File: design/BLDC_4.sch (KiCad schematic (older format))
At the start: 29 parts, among them K1 SERVO, P1 HALL, P101 CANBUS, P3 PWR_COMM/USART1/Encoder, P4 IN+, P5 IN-, P6 MOTOR1, P7 MOTOR2, P9 MOTOR3, X1 MINI-USB-SHIELD-32005-201

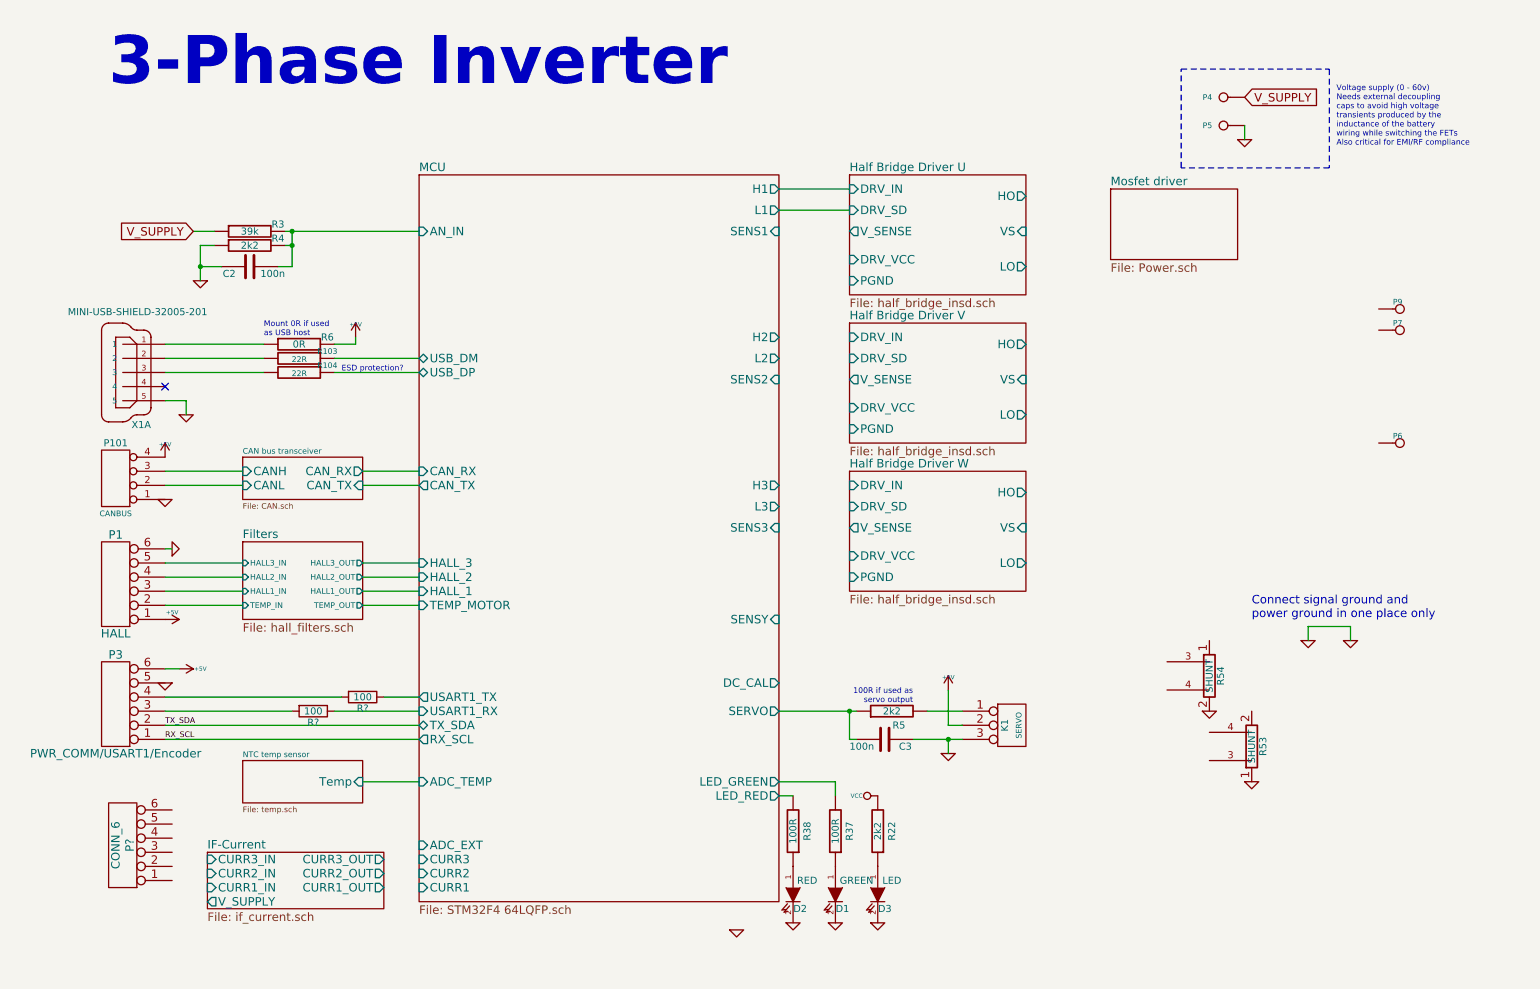
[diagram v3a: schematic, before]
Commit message: Removed 5V power level. Integrated isolated CAN bus driver.
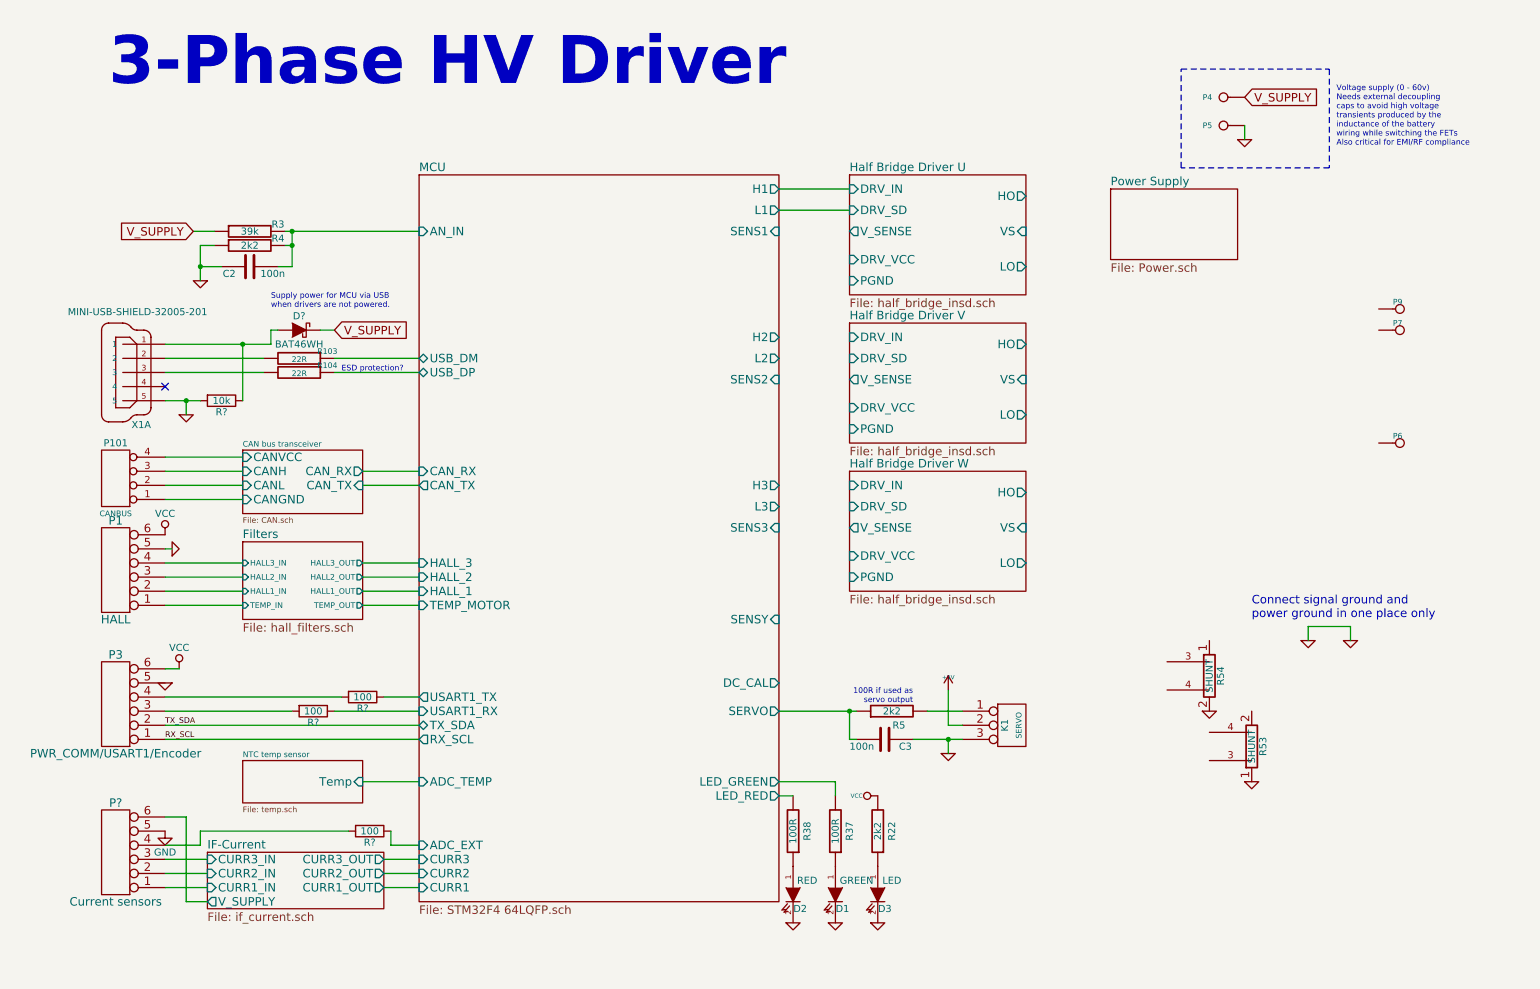
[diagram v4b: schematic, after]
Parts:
- removed R6: 0R, SMD_Packages:SMD-0603_r, symbol R-RESCUE-BLDC_4
- added D?: BAT46WH, symbol BAT46WH
- added R?: 100, symbol R
- added R?: 10k, symbol R
- P?: value CONN_6 -> Current sensors
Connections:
- net +5V: no longer P1.1, P101.4 (P4), P3.6
- net Filters/HALL1_IN: now also P1.2; no longer P1.3
- net Filters/HALL2_IN: now also P1.3; no longer P1.4
- net Filters/HALL3_IN: now also P1.4; no longer P1.5
- net Filters/TEMP_IN: now also P1.1; no longer P1.2
- net GND: now also P1.5, P?.5, R?.2; no longer P1.6, P101.1 (P1)
- net IF-Current/CURR1_IN: now also P?.1
- net IF-Current/CURR2_IN: now also P?.2
- net IF-Current/CURR3_IN: now also P?.3
- net IF-Current/V_SUPPLY: now also P?.6
- net MCU/ADC_EXT: now also R?.1
- net VCC: now also P1.6, P3.6
- net V_SUPPLY: now also D?.1 (K)
- net at X1.1: now also D?.2 (A), R?.1
- net at P?.4: now also R?.2
- new net CAN bus transceiver/CANGND: P101.1 (P1)
- new net CAN bus transceiver/CANVCC: P101.4 (P4)
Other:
- note added: "3-Phase HV Driver"
- note added: "Supply power for MCU via USB\nwhen drivers are not powered."
- note removed: "3-Phase Inverter"
- note removed: "Mount 0R if used\nas USB host"
- moved on the sheet: P1, P?
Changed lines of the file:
@@
 encoding utf-8
 Sheet 1 10
-Title "BLDC Driver 4.6"
-Date "25 Aug 2014"
-Rev "4.6"
-Comp "Benjamin Vedder"
+Title "3-Phase HV Driver"
+Date "2015-08-27"
+Rev "0.1"
+Comp "Jörg Wangemann"
 Comment1 ""
 Comment2 ""
@@
 L CONN_6 P1
 U 1 1 522DA047
-P 1100 4650
-F 0 "P1" H 1100 4300 60  0000 C CNN
-F 1 "HALL" H 1100 5000 60  0000 C CNN
-F 2 "CRF1:MICRO_JST_6" H 1100 4650 60  0001 C CNN
-F 3 "" H 1100 4650 60  0001 C CNN
-	1    1100 4650
+P 1100 4550
+F 0 "P1" H 1100 4200 60  0000 C CNN
+F 1 "HALL" H 1100 4900 60  0000 C CNN
+F 2 "CRF1:MICRO_JST_6" H 1100 4550 60  0001 C CNN
+F 3 "" H 1100 4550 60  0001 C CNN
+	1    1100 4550
 	-1   0    0    1
 $EndComp
 $Comp
-L +5V #PWR01
-U 1 1 522DA04D
-P 1450 4900
-F 0 "#PWR01" H 1450 4990 20  0001 C CNN
-F 1 "+5V" V 1400 4950 30  0000 C CNN
-F 2 "" H 1450 4900 60  0001 C CNN
-F 3 "" H 1450 4900 60  0001 C CNN
-	1    1450 4900
-	0    1    1    0
-$EndComp
-$Comp
 L GND-RESCUE-BLDC_4 #PWR02
 U 1 1 522DA053
@@
 $EndComp
 $Comp
-L +5V #PWR07
-U 1 1 522DA11A
-P 1550 5250
-F 0 "#PWR07" H 1550 5340 20  0001 C CNN
-F 1 "+5V" V 1550 5400 30  0000 C CNN
-F 2 "" H 1550 5250 60  0001 C CNN
-F 3 "" H 1550 5250 60  0001 C CNN
-	1    1550 5250
-	0    1    1    0
-$EndComp
-$Comp
 L +5V #PWR09
 U 1 1 522DA158
@@
 Text Notes 6750 5500 2    40   ~ 0
 100R if used as\nservo output
-$Comp
-L R-RESCUE-BLDC_4 R6
-U 1 1 522DA24E
-P 2400 2950
-F 0 "R6" V 2350 2750 50  0000 C CNN
-F 1 "0R" V 2400 2950 50  0000 C CNN
-F 2 "SMD_Packages:SMD-0603_r" H 2400 2950 60  0001 C CNN
-F 3 "" H 2400 2950 60  0001 C CNN
-	1    2400 2950
-	0    -1   1    0
-$EndComp
-$Comp
-L +5V #PWR010
-U 1 1 522DA254
-P 2800 2900
-F 0 "#PWR010" H 2800 2990 20  0001 C CNN
-F 1 "+5V" H 2800 2990 30  0000 C CNN
-F 2 "" H 2800 2900 60  0001 C CNN
-F 3 "" H 2800 2900 60  0001 C CNN
-	1    2800 2900
-	1    0    0    -1
-$EndComp
-Text Notes 2150 2900 0    40   ~ 0
-Mount 0R if used\nas USB host
+Text Notes 2200 2700 0    40   ~ 0
+Supply power for MCU via USB\nwhen drivers are not powered.
 Text Notes 2700 3150 0    40   ~ 0
 ESD protection?\n
@@
 TX_SDA
 Text Notes 1050 1150 0    340  ~ 68
-3-Phase Inverter
+3-Phase HV Driver
 $Bitmap
 Pos 10700 3200
@@
 $EndSheet
 $Sheet
-S 2000 3750 850  300
+S 2000 3700 850  450
 U 53FFB6E1
 F0 "CAN bus transceiver" 40
@@
 F4 "CANH" I L 2000 3850 60
 F5 "CANL" I L 2000 3950 60
+F6 "CANGND" I L 2000 4050 60
+F7 "CANVCC" I L 2000 3750 60
 $EndSheet
-$Comp
-L GND-RESCUE-BLDC_4 #PWR012
-U 1 1 53FB6DA8
-P 1450 4050
-F 0 "#PWR012" H 1450 4050 30  0001 C CNN
-F 1 "GND" H 1450 3980 30  0001 C CNN
-F 2 "" H 1450 4050 60  0001 C CNN
-F 3 "" H 1450 4050 60  0001 C CNN
-	1    1450 4050
-	1    0    0    -1
-$EndComp
 $Sheet
 S 2000 4350 850  550
@@
 	1550 5250 1450 5250
 Wire Wire Line
-	1600 3350 1450 3350
+	1450 3350 1700 3350
 Wire Wire Line
 	1600 3450 1600 3350
@@
 	1450 4400 1500 4400
 Wire Wire Line
-	2800 2900 2800 2950
-Wire Wire Line
-	2150 2950 1450 2950
-Wire Wire Line
 	9550 4950 9550 5050
 Wire Wire Line
@@
 	1450 5650 3250 5650
 Wire Wire Line
-	1450 3950 2000 3950
-Wire Wire Line
-	1450 3850 2000 3850
-Wire Wire Line
 	1450 4500 2000 4500
 Wire Wire Line
@@
 	3250 4800 2850 4800
 Wire Wire Line
-	2850 3850 3250 3850
-Wire Wire Line
-	3250 3950 2850 3950
-Wire Wire Line
 	2150 3050 1450 3050
 Wire Wire Line
@@
 Wire Wire Line
 	7000 5650 7000 5400
-Wire Wire Line
-	2800 2950 2650 2950
 $Comp
 L CONN_4 P101
@@
 	-1   0    0    1
 $EndComp
-$Comp
-L +5V #PWR017
-U 1 1 54036995
-P 1450 3750
-F 0 "#PWR017" H 1450 3840 20  0001 C CNN
-F 1 "+5V" H 1450 3840 30  0000 C CNN
-F 2 "" H 1450 3750 60  0001 C CNN
-F 3 "" H 1450 3750 60  0001 C CNN
-	1    1450 3750
-	1    0    0    -1
-$EndComp
 Wire Wire Line
 	9550 4950 9850 4950
@@
 $EndComp
 $Comp
-L GND-RESCUE-BLDC_4 #PWR021
-U 1 1 548F254E
-P 5500 7100
-F 0 "#PWR021" H 5500 7100 30  0001 C CNN
-F 1 "GND" H 5500 7030 30  0001 C CNN
-F 2 "" H 5500 7100 60  0001 C CNN
-F 3 "" H 5500 7100 60  0001 C CNN
-	1    5500 7100
-	1    0    0    -1
-$EndComp
-$Comp
 L GND-RESCUE-BLDC_4 #PWR022
 U 1 1 548F2573
@@
 L CONN_6 P?
 U 1 1 56060A2F
-P 1150 6500
-F 0 "P?" V 1100 6500 60  0000 C CNN
-F 1 "CONN_6" V 1200 6500 60  0000 C CNN
-F 2 "" H 1150 6500 60  0000 C CNN
-F 3 "" H 1150 6500 60  0000 C CNN
-	1    1150 6500
+P 1100 6550
+F 0 "P?" H 1100 6200 60  0000 C CNN
+F 1 "Current sensors" H 1100 6900 60  0000 C CNN
+F 2 "" H 1100 6550 60  0000 C CNN
+F 3 "" H 1100 6550 60  0000 C CNN
+	1    1100 6550
 	-1   0    0    1
 $EndComp
@@
 S 8150 1850 900  500
 U 504F83BE
-F0 "Mosfet driver" 60
+F0 "Power Supply" 60
 F1 "Power.sch" 60
 $EndSheet
@@
 F8 "V_SUPPLY" O L 1750 6900 60
 $EndSheet
+$Comp
+L R R?
+U 1 1 55DFBA3B
+P 2900 6400
+F 0 "R?" V 2980 6400 50  0000 C CNN
+F 1 "100" V 2900 6400 50  0000 C CNN
+F 2 "" V 2830 6400 30  0000 C CNN
+F 3 "" H 2900 6400 30  0000 C CNN
+	1    2900 6400
+	0    1    1    0
+$EndComp
+Wire Wire Line
+	1450 6800 1750 6800
+Wire Wire Line
+	1450 6700 1750 6700
+Wire Wire Line
+	1450 6600 1750 6600
+Wire Wire Line
+	1450 6500 1700 6500
+Wire Wire Line
+	1700 6500 1700 6400
+Wire Wire Line
+	1700 6400 2750 6400
+Wire Wire Line
+	3050 6400 3050 6500
+Wire Wire Line
+	3050 6500 3250 6500
+Wire Wire Line
+	3000 6600 3250 6600
+Wire Wire Line
+	3000 6700 3250 6700
+Wire Wire Line
+	3000 6800 3250 6800
+$Comp
+L GND #PWR?
+U 1 1 55DFDF4F
+P 1450 6400
+F 0 "#PWR?" H 1450 6150 50  0001 C CNN
+F 1 "GND" H 1450 6250 50  0000 C CNN
+F 2 "" H 1450 6400 60  0000 C CNN
+F 3 "" H 1450 6400 60  0000 C CNN
+	1    1450 6400
+	1    0    0    -1
+$EndComp
+Wire Wire Line
+	1750 6900 1600 6900
+Wire Wire Line
+	1600 6900 1600 6300
+Wire Wire Line
+	1600 6300 1450 6300
+$Comp
+L BAT46WH D?
+U 1 1 55DFBB15
+P 2400 2850
+F 0 "D?" H 2400 2950 50  0000 C CNN
+F 1 "BAT46WH" H 2400 2750 50  0000 C CNN
+F 2 "" H 2400 2850 60  0000 C CNN
+F 3 "" H 2400 2850 60  0000 C CNN
+	1    2400 2850
+	-1   0    0    -1
+$EndComp
+Wire Wire Line
+	1450 2950 2200 2950
+Wire Wire Line
+	2200 2950 2200 2850
+Wire Wire Line
+	2200 2850 2250 2850
+$Comp
+L R R?
+U 1 1 55DFC8FE
+P 1850 3350
+F 0 "R?" V 1930 3350 50  0000 C CNN
+F 1 "10k" V 1850 3350 50  0000 C CNN
+F 2 "" V 1780 3350 30  0000 C CNN
+F 3 "" H 1850 3350 30  0000 C CNN
+	1    1850 3350
+	0    1    1    0
+$EndComp
+Connection ~ 1600 3350
+Wire Wire Line
+	2000 3350 2000 2950
+Connection ~ 2000 2950
+Text GLabel 2650 2850 2    60   Input ~ 0
+V_SUPPLY
+Wire Wire Line
+	2550 2850 2650 2850
+$Comp
+L VCC #PWR?
+U 1 1 55E0BF1D
+P 1450 4300
+F 0 "#PWR?" H 1450 4150 50  0001 C CNN
+F 1 "VCC" H 1450 4450 50  0000 C CNN
+F 2 "" H 1450 4300 60  0000 C CNN
+F 3 "" H 1450 4300 60  0000 C CNN
+	1    1450 4300
+	1    0    0    -1
+$EndComp
+$Comp
+L VCC #PWR?
+U 1 1 55E0C570
+P 1550 5250
+F 0 "#PWR?" H 1550 5100 50  0001 C CNN
+F 1 "VCC" H 1550 5400 50  0000 C CNN
+F 2 "" H 1550 5250 60  0000 C CNN
+F 3 "" H 1550 5250 60  0000 C CNN
+	1    1550 5250
+	1    0    0    -1
+$EndComp
+Wire Wire Line
+	2850 3850 3250 3850
+Wire Wire Line
+	3250 3950 2850 3950
+Wire Wire Line
+	1450 3850 2000 3850
+Wire Wire Line
+	1450 3950 2000 3950
+Wire Wire Line
+	1450 3750 2000 3750
+Wire Wire Line
+	1450 4050 2000 4050
 $EndSCHEMATC

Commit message: First complete draft of the schematics.
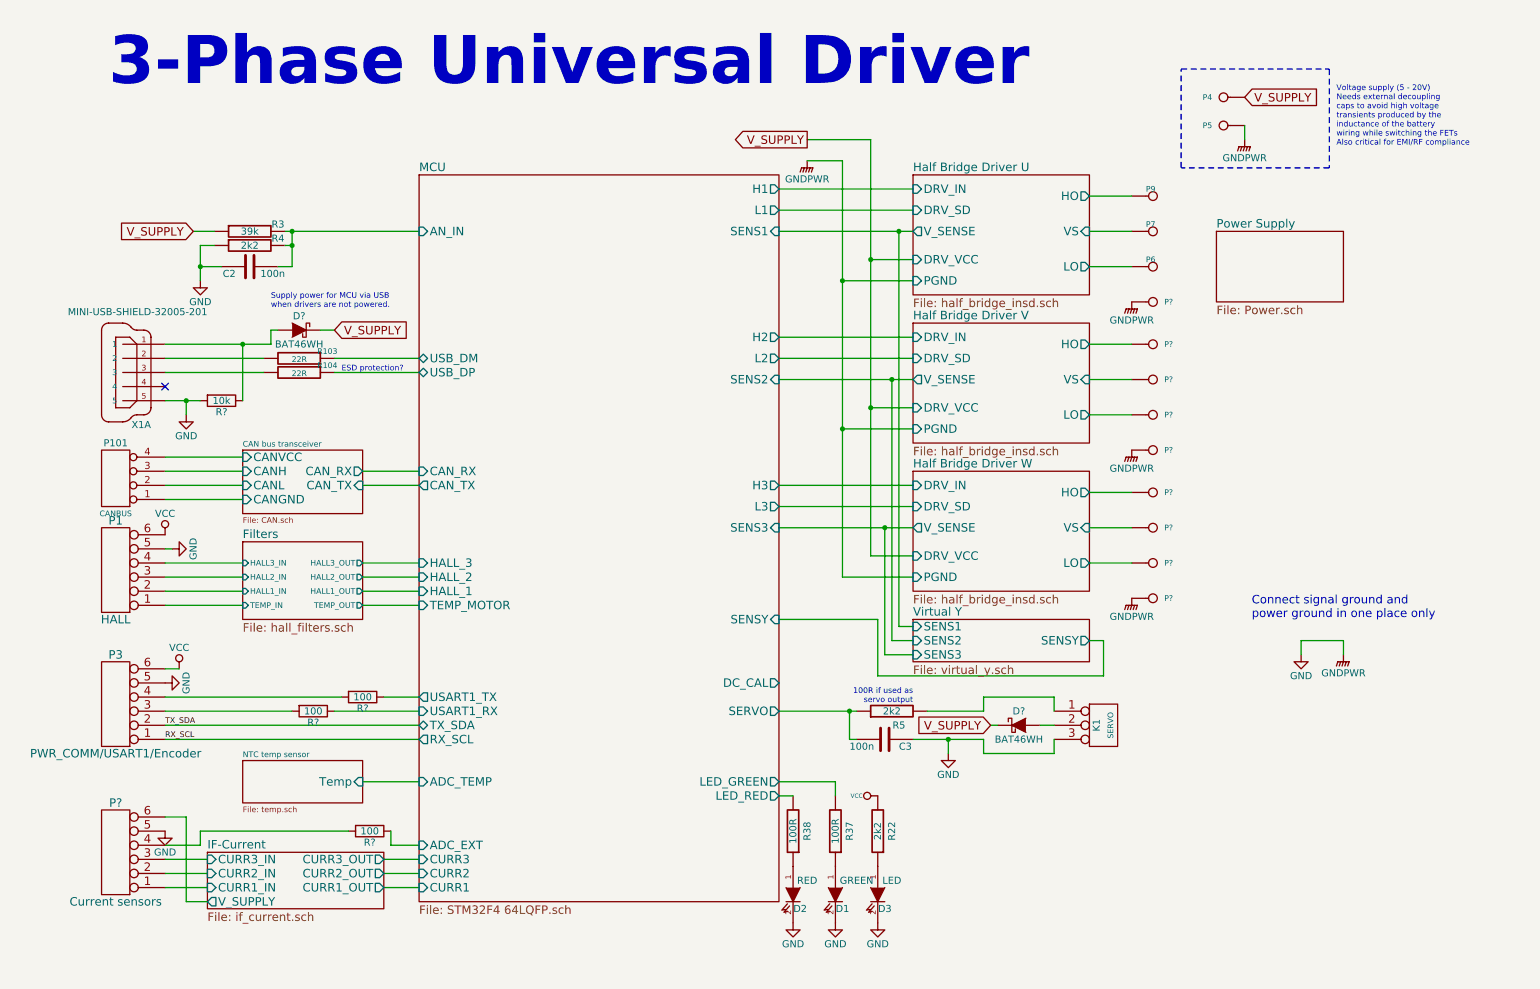
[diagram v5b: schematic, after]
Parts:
- removed R53, R54: SHUNT, CRF1:WSLP2726, symbol SHUNT
- added D?: BAT46WH, symbol BAT46WH
- added P? (x9): CONN_1, symbol CONN_1
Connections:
- net GND: now also P?.1, P?.1, P?.1
- net Half Bridge Driver U/HO: now also P9.1
- net Half Bridge Driver U/LO: now also P6.1
- net Half Bridge Driver U/VS: now also P7.1
- net Half Bridge Driver V/HO: now also P?.1
- net Half Bridge Driver V/LO: now also P?.1
- net Half Bridge Driver V/VS: now also P?.1
- net Half Bridge Driver W/HO: now also P?.1
- net Half Bridge Driver W/LO: now also P?.1
- net Half Bridge Driver W/VS: now also P?.1
- net V_SUPPLY: now also D?.1 (K)
- net +5V: no longer names the net of K1.2 (PM)
- net +5V: now also D?.2 (A)
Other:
- note added: "3-Phase Universal Driver"
- note added: "Voltage supply (5 - 20V)\nNeeds external decoupling\ncaps to avoid high voltage\ntransients produced by the\ninductance of the battery\nwiring while switching the FETs\nAlso critical for EMI/RF compliance"
- note removed: "3-Phase HV Driver"
- note removed: "Voltage supply (0 - 60v)\nNeeds external decoupling\ncaps to avoid high voltage\ntransients produced by the\ninductance of the battery\nwiring while switching the FETs\nAlso critical for EMI/RF compliance"
- moved on the sheet: K1, P6, P7, P9

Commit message: Assigned some footprints.
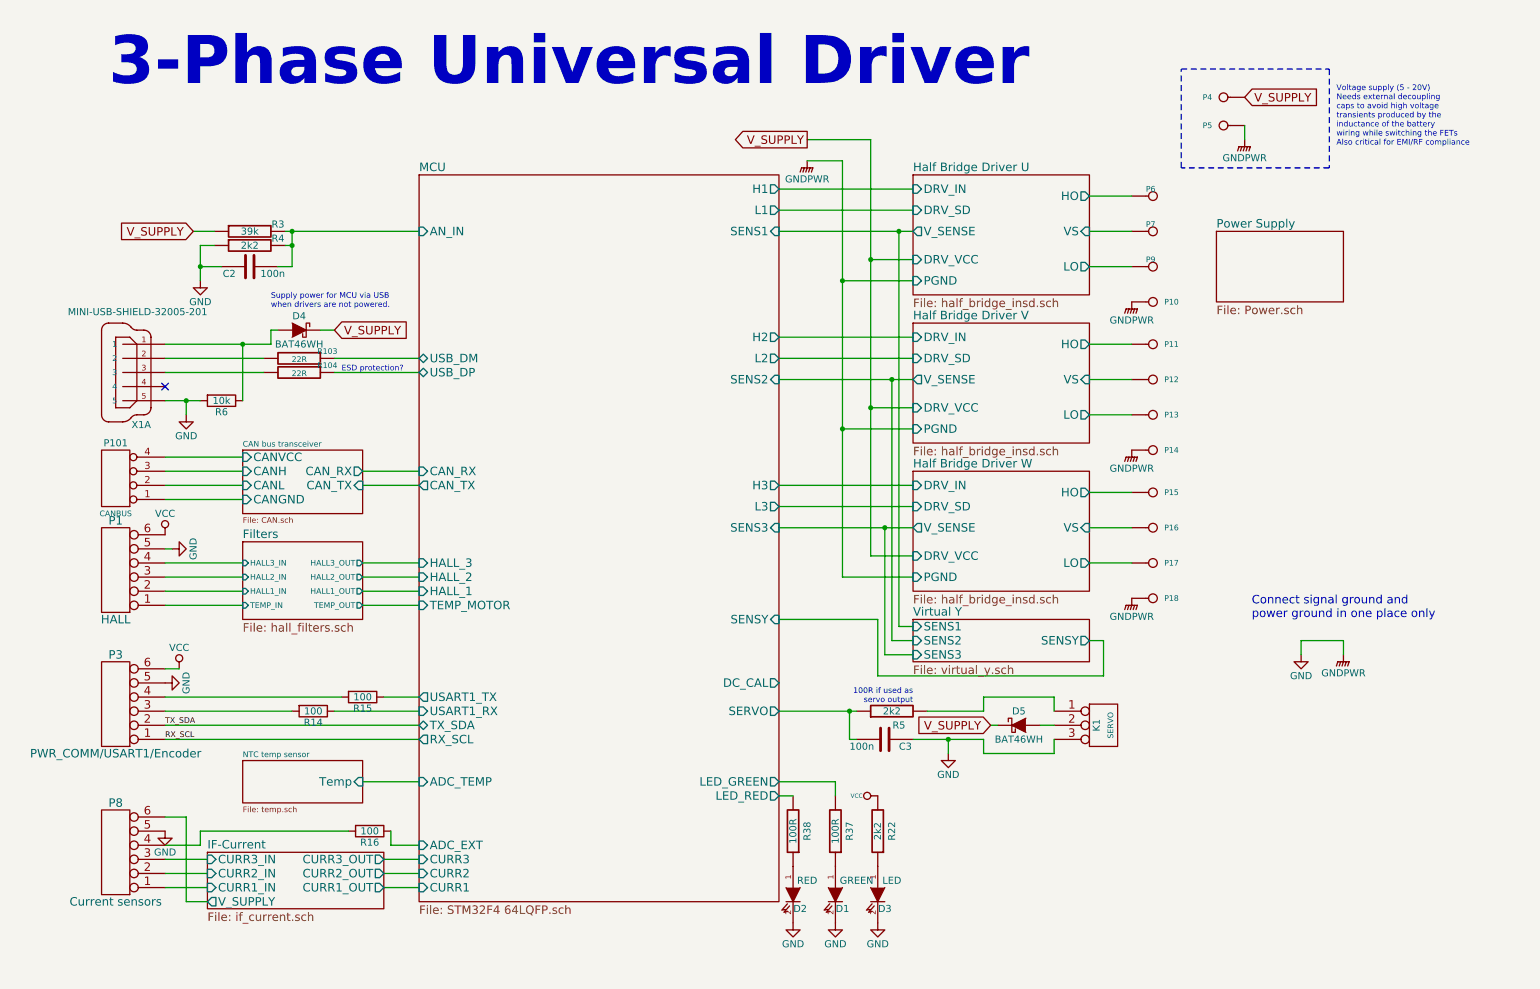
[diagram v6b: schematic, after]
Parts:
- C2, C3: footprint SMD_Packages:SMD-0603_c -> Capacitors_SMD:C_0603
- D4, D5: renamed from D?; footprint (none) -> Diodes_SMD:SOD-123
- gave numbers to parts that had none: 14
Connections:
- net Half Bridge Driver U/HO: now also P6.1; no longer P9.1
- net Half Bridge Driver U/LO: now also P9.1; no longer P6.1
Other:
- moved on the sheet: P6, P9
